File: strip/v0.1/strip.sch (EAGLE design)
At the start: 101 parts, among them IC1 LP2992, IC2 ADP3110A-SO8, IC3 MAX3051, IC4 OPA335, IC5 ADP3110A-SO8, IC6 ADP3110A-SO8, IC7 STM32F050CX, Q1 IRF7828, Q2 IRF7828, Q3 IRF7828, Q4 IRF7828, Q5 IRF7828, Q6 IRF7828

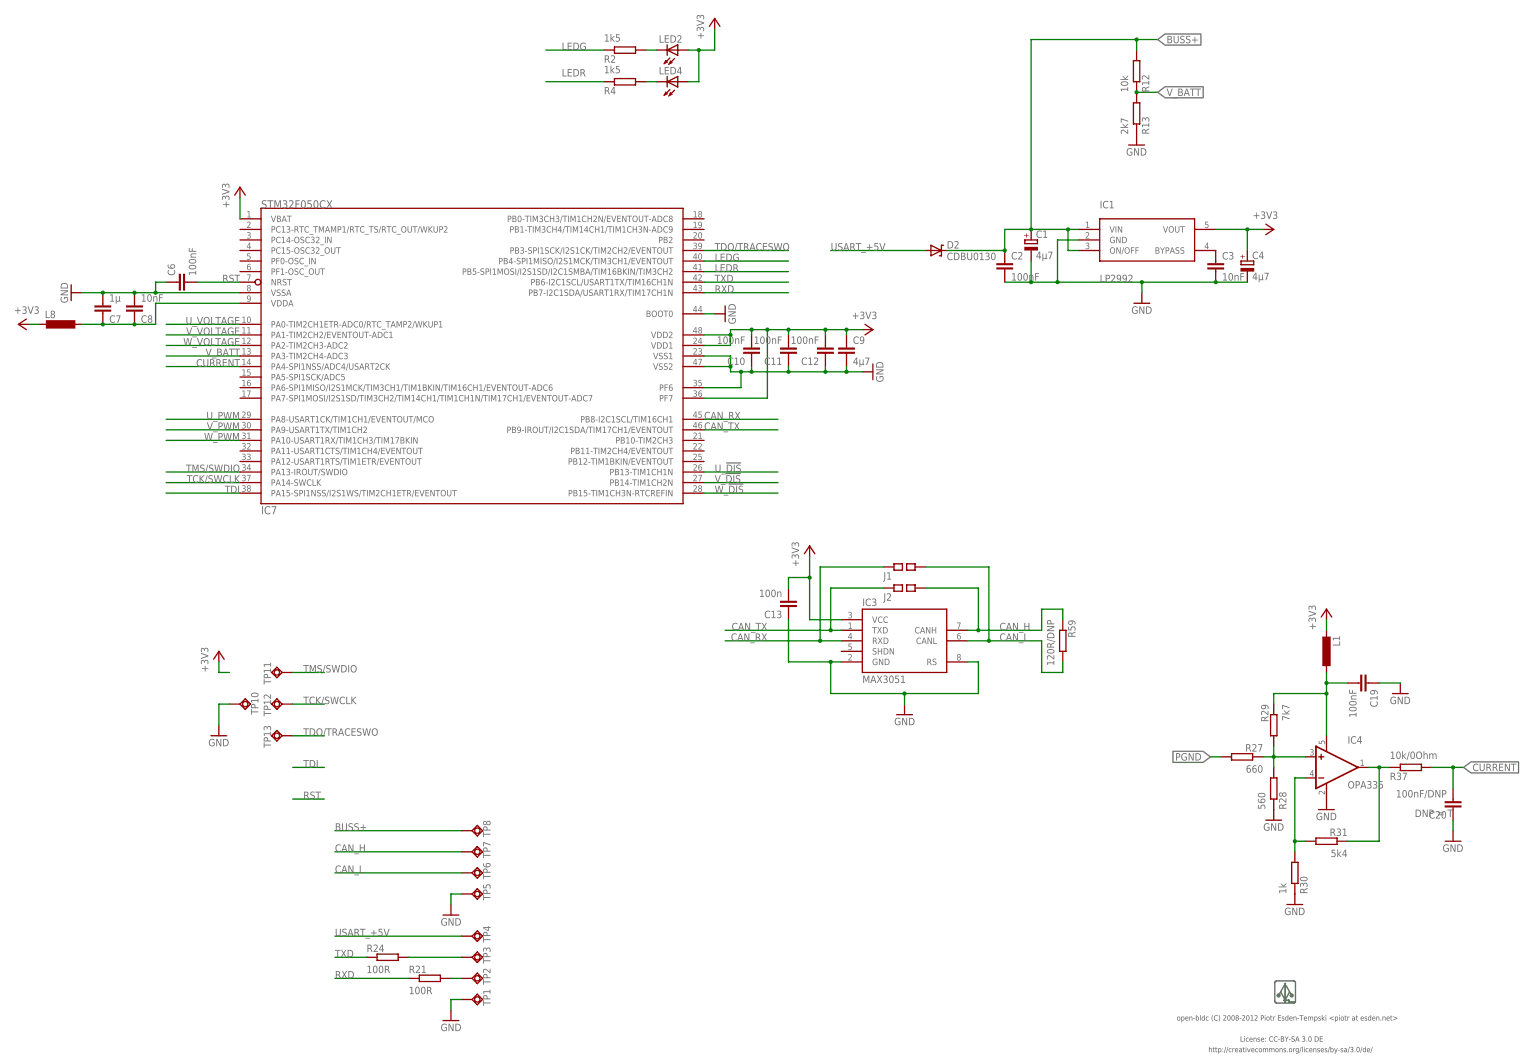
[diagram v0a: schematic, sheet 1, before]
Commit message: Added jumper to (dis)connect BUSS+ and V_IN.
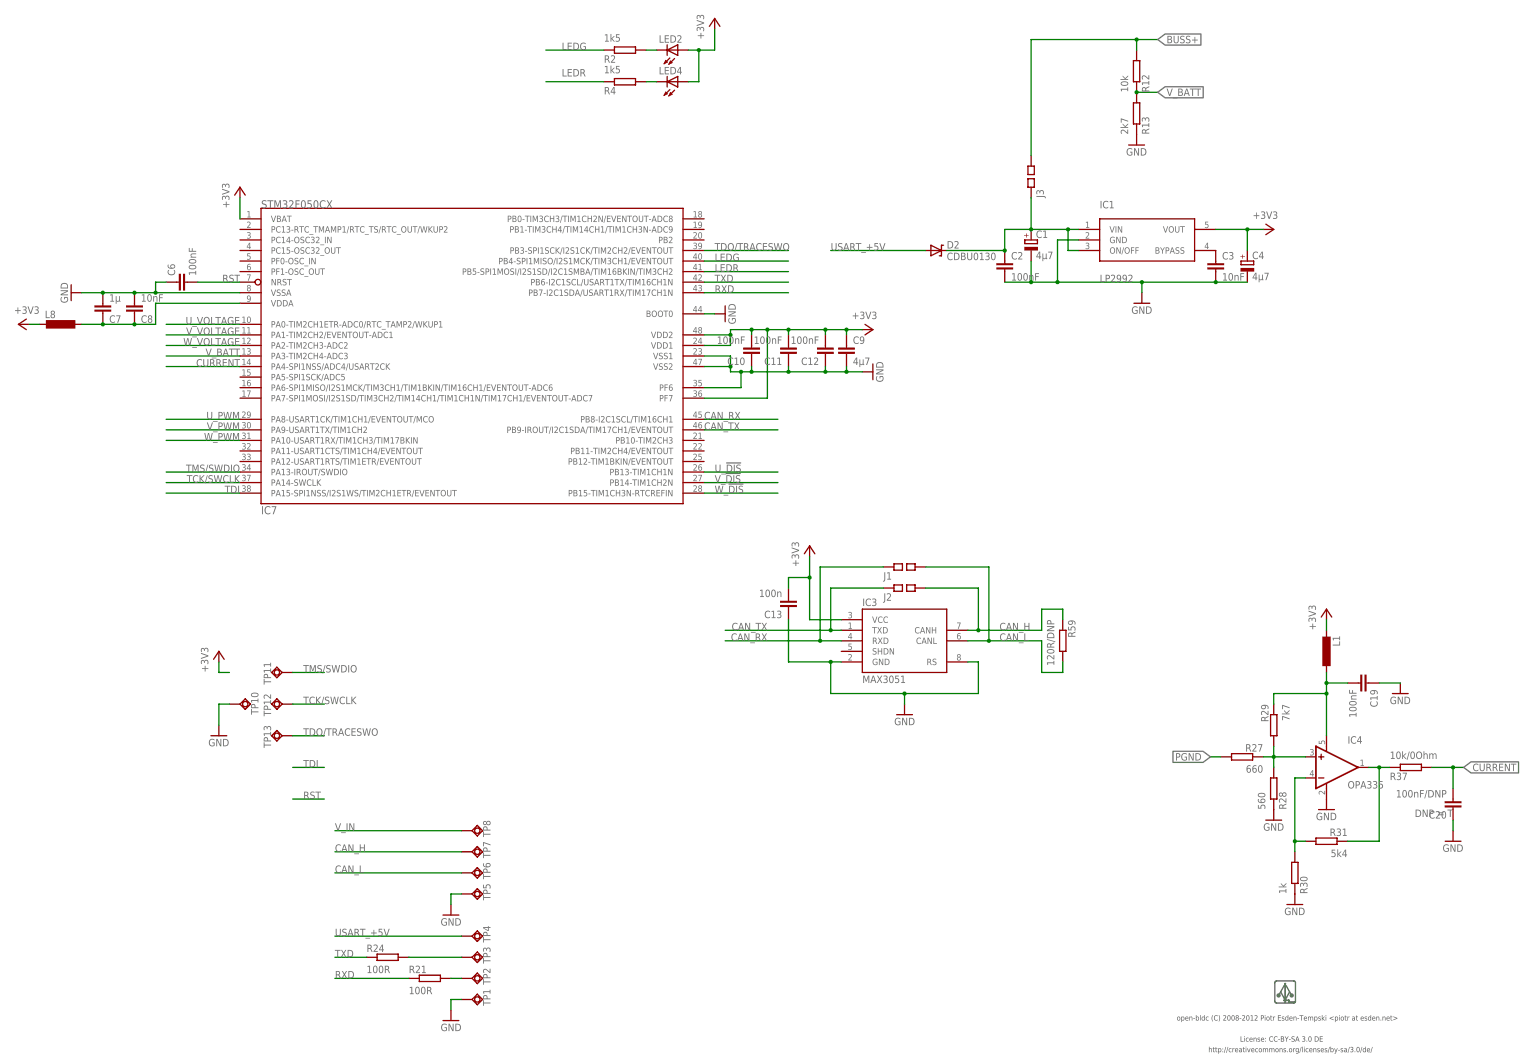
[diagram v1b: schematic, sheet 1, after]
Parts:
- added J3: (no value), pel_jumpers:SQ_JMP-0402
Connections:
- new net V_IN: C1.+, C2.1, D2.C, IC1.ON/OFF, IC1.VIN, J3.1, TP8.TP
- net BUSS+: now also J3.2; no longer C1.+, C2.1, D2.C, IC1.ON/OFF, IC1.VIN, TP8.TP
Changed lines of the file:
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@@
 <part name="J1" library="pel_jumpers" deviceset="SQ_JMP" device="-0402"/>
 <part name="J2" library="pel_jumpers" deviceset="SQ_JMP" device="-0402"/>
+<part name="J3" library="pel_jumpers" deviceset="SQ_JMP" device="-0402"/>
 </parts>
 <sheets>
@@
 <instance part="J1" gate="G$1" x="223.52" y="121.92"/>
 <instance part="J2" gate="G$1" x="223.52" y="116.84"/>
+<instance part="J3" gate="G$1" x="254" y="215.9" rot="R90"/>
 </instances>
 <busses>
@@
 <label x="284.48" y="248.92" size="1.778" layer="95" xref="yes"/>
 <pinref part="R12" gate="G$1" pin="2"/>
-<wire x1="233.68" y1="198.12" x2="247.65" y2="198.12" width="0.1524" layer="91"/>
-<wire x1="247.65" y1="198.12" x2="247.65" y2="203.2" width="0.1524" layer="91"/>
-<wire x1="247.65" y1="203.2" x2="254" y2="203.2" width="0.1524" layer="91"/>
-<wire x1="262.89" y1="198.12" x2="265.43" y2="198.12" width="0.1524" layer="91"/>
-<wire x1="265.43" y1="203.2" x2="262.89" y2="203.2" width="0.1524" layer="91"/>
-<wire x1="262.89" y1="203.2" x2="262.89" y2="198.12" width="0.1524" layer="91"/>
-<wire x1="254" y1="203.2" x2="262.89" y2="203.2" width="0.1524" layer="91"/>
-<junction x="247.65" y="198.12"/>
-<junction x="254" y="203.2"/>
-<junction x="262.89" y="203.2"/>
-<pinref part="C1" gate="G$1" pin="+"/>
-<pinref part="D2" gate="G$1" pin="C"/>
-<pinref part="C2" gate="G$1" pin="1"/>
-<pinref part="IC1" gate="G$1" pin="ON/OFF"/>
-<pinref part="IC1" gate="G$1" pin="VIN"/>
-<wire x1="254" y1="248.92" x2="254" y2="203.2" width="0.1524" layer="91"/>
-</segment>
-<segment>
-<pinref part="TP8" gate="G$1" pin="TP"/>
-<wire x1="116.84" y1="58.42" x2="86.36" y2="58.42" width="0.1524" layer="91"/>
-<label x="86.36" y="58.42" size="1.778" layer="95"/>
+<wire x1="254" y1="248.92" x2="254" y2="220.98" width="0.1524" layer="91"/>
+<pinref part="J3" gate="G$1" pin="2"/>
 </segment>
 </net>
@@
 </segment>
 </net>
+<net name="V_IN" class="0">
+<segment>
+<pinref part="IC1" gate="G$1" pin="ON/OFF"/>
+<wire x1="262.89" y1="198.12" x2="265.43" y2="198.12" width="0.1524" layer="91"/>
+<pinref part="IC1" gate="G$1" pin="VIN"/>
+<wire x1="265.43" y1="203.2" x2="262.89" y2="203.2" width="0.1524" layer="91"/>
+<wire x1="262.89" y1="203.2" x2="262.89" y2="198.12" width="0.1524" layer="91"/>
+<junction x="262.89" y="203.2"/>
+<wire x1="254" y1="203.2" x2="262.89" y2="203.2" width="0.1524" layer="91"/>
+<junction x="254" y="203.2"/>
+<pinref part="C1" gate="G$1" pin="+"/>
+<pinref part="J3" gate="G$1" pin="1"/>
+<wire x1="254" y1="210.82" x2="254" y2="203.2" width="0.1524" layer="91"/>
+<wire x1="247.65" y1="203.2" x2="254" y2="203.2" width="0.1524" layer="91"/>
+<wire x1="247.65" y1="198.12" x2="247.65" y2="203.2" width="0.1524" layer="91"/>
+<junction x="247.65" y="198.12"/>
+<pinref part="C2" gate="G$1" pin="1"/>
+<wire x1="233.68" y1="198.12" x2="247.65" y2="198.12" width="0.1524" layer="91"/>
+<pinref part="D2" gate="G$1" pin="C"/>
+</segment>
+<segment>
+<pinref part="TP8" gate="G$1" pin="TP"/>
+<wire x1="116.84" y1="58.42" x2="86.36" y2="58.42" width="0.1524" layer="91"/>
+<label x="86.36" y="58.42" size="1.778" layer="95"/>
+</segment>
+</net>

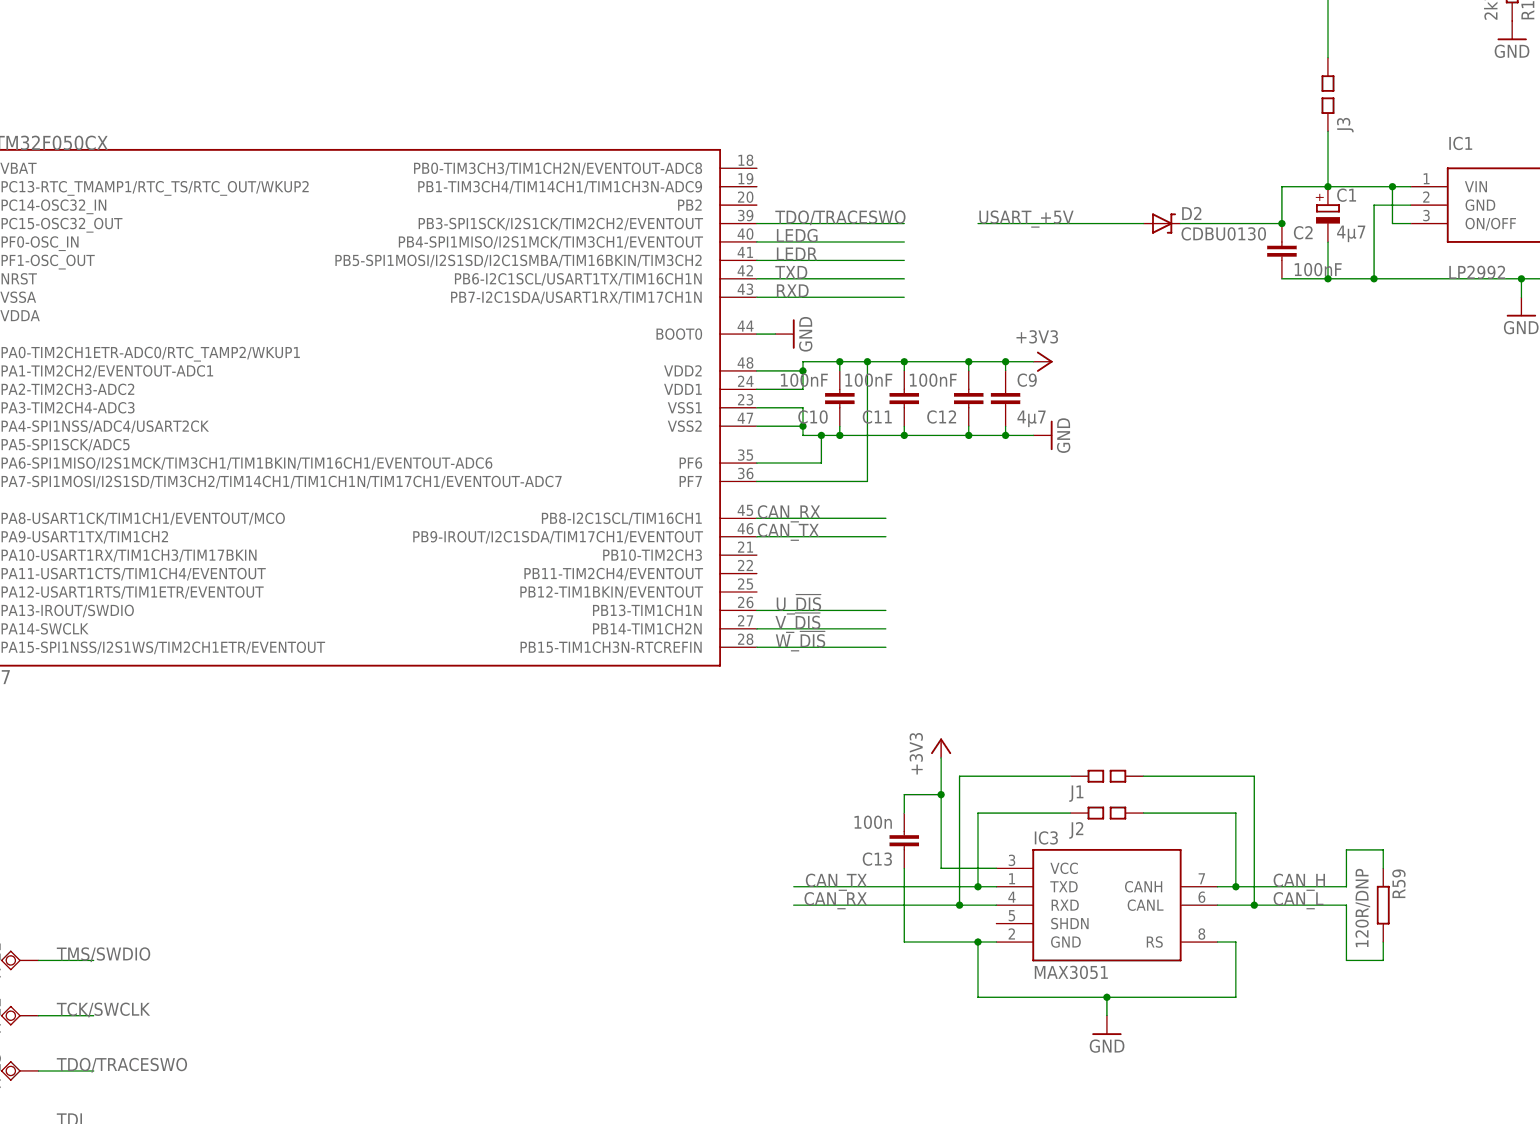
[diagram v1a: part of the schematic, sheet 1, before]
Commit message: More work on the BOM and part documentation.
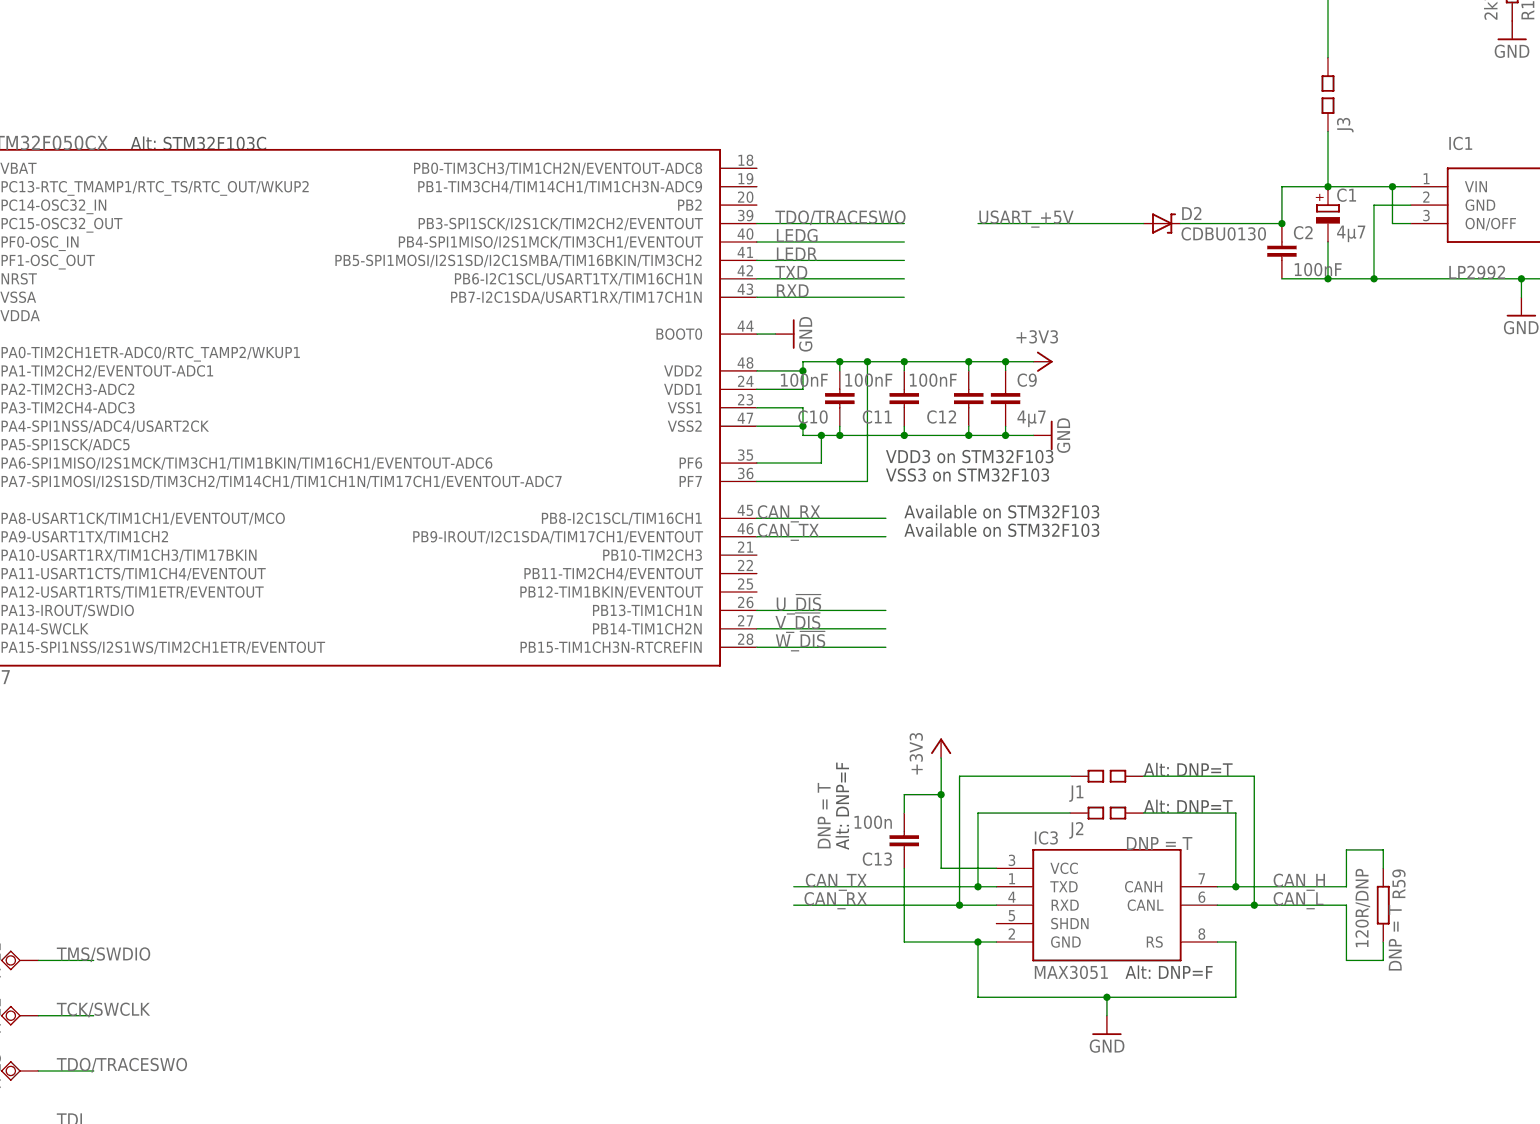
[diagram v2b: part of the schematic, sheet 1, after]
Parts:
- C13, R59: DNP (none) -> T
- IC3: DNP (none) -> T; PARTNO (none) -> *
- J1, J2, J3: PARTNO (none) -> res-0402-0
- L2, L3, L4, L5, L6, L7: PARTNO * -> res-0402-0
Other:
- note added: "Alt: DNP=F"
- note added: "Alt: DNP=T"
- note added: "Alt: STM32F103C"
- note added: "Available on STM32F103"
- note added: "VDD3 on STM32F103"
- note added: "VSS3 on STM32F103"
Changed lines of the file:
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@@
 </part>
 <part name="L2" library="pel_dipol_comp" deviceset="INDUCTOR" device="-0402">
-<attribute name="PARTNO" value="*"/>
+<attribute name="PARTNO" value="res-0402-0"/>
 </part>
 <part name="L3" library="pel_dipol_comp" deviceset="INDUCTOR" device="-0402">
-<attribute name="PARTNO" value="*"/>
+<attribute name="PARTNO" value="res-0402-0"/>
 </part>
 <part name="L4" library="pel_dipol_comp" deviceset="INDUCTOR" device="-0402">
-<attribute name="PARTNO" value="*"/>
+<attribute name="PARTNO" value="res-0402-0"/>
 </part>
 <part name="L5" library="pel_dipol_comp" deviceset="INDUCTOR" device="-0402">
-<attribute name="PARTNO" value="*"/>
+<attribute name="PARTNO" value="res-0402-0"/>
 </part>
 <part name="L6" library="pel_dipol_comp" deviceset="INDUCTOR" device="-0402">
-<attribute name="PARTNO" value="*"/>
+<attribute name="PARTNO" value="res-0402-0"/>
 </part>
 <part name="L7" library="pel_dipol_comp" deviceset="INDUCTOR" device="-0402">
-<attribute name="PARTNO" value="*"/>
+<attribute name="PARTNO" value="res-0402-0"/>
 </part>
 <part name="Q1" library="open-bldc" deviceset="IRF7828" device="">
@@
 </part>
 <part name="C13" library="pel_dipol_comp" deviceset="CAPACITOR" device="-0402" value="100n">
+<attribute name="DNP" value="T"/>
 <attribute name="PARTNO" value="cap-cer-0402-100n"/>
 </part>
 <part name="R59" library="pel_dipol_comp" deviceset="RESISTOR" device="-0402" value="120R/DNP">
+<attribute name="DNP" value="T"/>
 <attribute name="PARTNO" value="res-0402-60.4"/>
 </part>
-<part name="IC3" library="open-bldc" deviceset="MAX3051" device=""/>
+<part name="IC3" library="open-bldc" deviceset="MAX3051" device="">
+<attribute name="DNP" value="T"/>
+<attribute name="PARTNO" value="*"/>
+</part>
 <part name="GND4" library="supply1" deviceset="GND" device=""/>
 <part name="P+4" library="supply1" deviceset="+3V3" device=""/>
-<part name="J1" library="pel_jumpers" deviceset="SQ_JMP" device="-0402"/>
-<part name="J2" library="pel_jumpers" deviceset="SQ_JMP" device="-0402"/>
-<part name="J3" library="pel_jumpers" deviceset="SQ_JMP" device="-0402"/>
+<part name="J1" library="pel_jumpers" deviceset="SQ_JMP" device="-0402">
+<attribute name="PARTNO" value="res-0402-0"/>
+</part>
+<part name="J2" library="pel_jumpers" deviceset="SQ_JMP" device="-0402">
+<attribute name="PARTNO" value="res-0402-0"/>
+</part>
+<part name="J3" library="pel_jumpers" deviceset="SQ_JMP" device="-0402">
+<attribute name="PARTNO" value="res-0402-0"/>
+</part>
 </parts>
 <sheets>
@@
 <text x="296.672" y="5.08" size="1.27" layer="97">http://creativecommons.org/licenses/by-sa/3.0/de/</text>
 <text x="289.052" y="12.7" size="1.27" layer="97">open-bldc (C) 2008-2012 Piotr Esden-Tempski &lt;piotr at esden.net&gt;</text>
+<text x="193.04" y="165.1" size="1.778" layer="97">VDD3 on STM32F103</text>
+<text x="193.04" y="162.56" size="1.778" layer="97">VSS3 on STM32F103</text>
+<text x="195.58" y="157.48" size="1.778" layer="97">Available on STM32F103</text>
+<text x="195.58" y="154.94" size="1.778" layer="97">Available on STM32F103</text>
+<text x="88.9" y="208.28" size="1.778" layer="97">Alt: STM32F103C</text>
+<text x="228.6" y="121.92" size="1.778" layer="97">Alt: DNP=T</text>
+<text x="228.6" y="116.84" size="1.778" layer="97">Alt: DNP=T</text>
+<text x="226.06" y="93.98" size="1.778" layer="97">Alt: DNP=F</text>
+<text x="187.96" y="111.76" size="1.778" layer="97" rot="R90">Alt: DNP=F</text>
 </plain>
 <instances>
@@
 <instance part="C13" gate="G$1" x="195.58" y="111.76" rot="R180">
 <attribute name="PARTNO" x="195.58" y="111.76" size="1.778" layer="96" rot="MR270" display="off"/>
+<attribute name="DNP" x="185.42" y="111.76" size="1.778" layer="96" rot="R90" display="both"/>
 </instance>
 <instance part="R59" gate="G$1" x="261.62" y="104.14" rot="MR270">
 <attribute name="PARTNO" x="261.62" y="104.14" size="1.778" layer="96" rot="MR0" display="off"/>
-</instance>
-<instance part="IC3" gate="G$1" x="223.52" y="104.14"/>
+<attribute name="DNP" x="264.16" y="104.14" size="1.778" layer="96" rot="MR270" display="both"/>
+</instance>
+<instance part="IC3" gate="G$1" x="223.52" y="104.14">
+<attribute name="DNP" x="226.06" y="111.76" size="1.778" layer="96" display="both"/>
+<attribute name="PARTNO" x="223.52" y="104.14" size="1.778" layer="96" rot="R90" display="off"/>
+</instance>
 <instance part="GND4" gate="1" x="223.52" y="86.36" rot="MR0"/>
 <instance part="P+4" gate="G$1" x="200.66" y="127"/>
-<instance part="J1" gate="G$1" x="223.52" y="121.92"/>
-<instance part="J2" gate="G$1" x="223.52" y="116.84"/>
-<instance part="J3" gate="G$1" x="254" y="215.9" rot="R90"/>
+<instance part="J1" gate="G$1" x="223.52" y="121.92">
+<attribute name="PARTNO" x="223.52" y="121.92" size="1.778" layer="96" rot="R90" display="off"/>
+</instance>
+<instance part="J2" gate="G$1" x="223.52" y="116.84">
+<attribute name="PARTNO" x="223.52" y="116.84" size="1.778" layer="96" rot="R90" display="off"/>
+</instance>
+<instance part="J3" gate="G$1" x="254" y="215.9" rot="R90">
+<attribute name="PARTNO" x="254" y="215.9" size="1.778" layer="96" rot="R90" display="off"/>
+</instance>
 </instances>
 <busses>
